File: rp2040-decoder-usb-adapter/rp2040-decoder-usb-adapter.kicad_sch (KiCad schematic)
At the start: 14 parts, among them J1 505070-2422, J2 SWD, J3 SPEAKER, J4 MISC1, J8 RAIL_PADS, P1 USB_C_Receptacle_USB2.0_16P

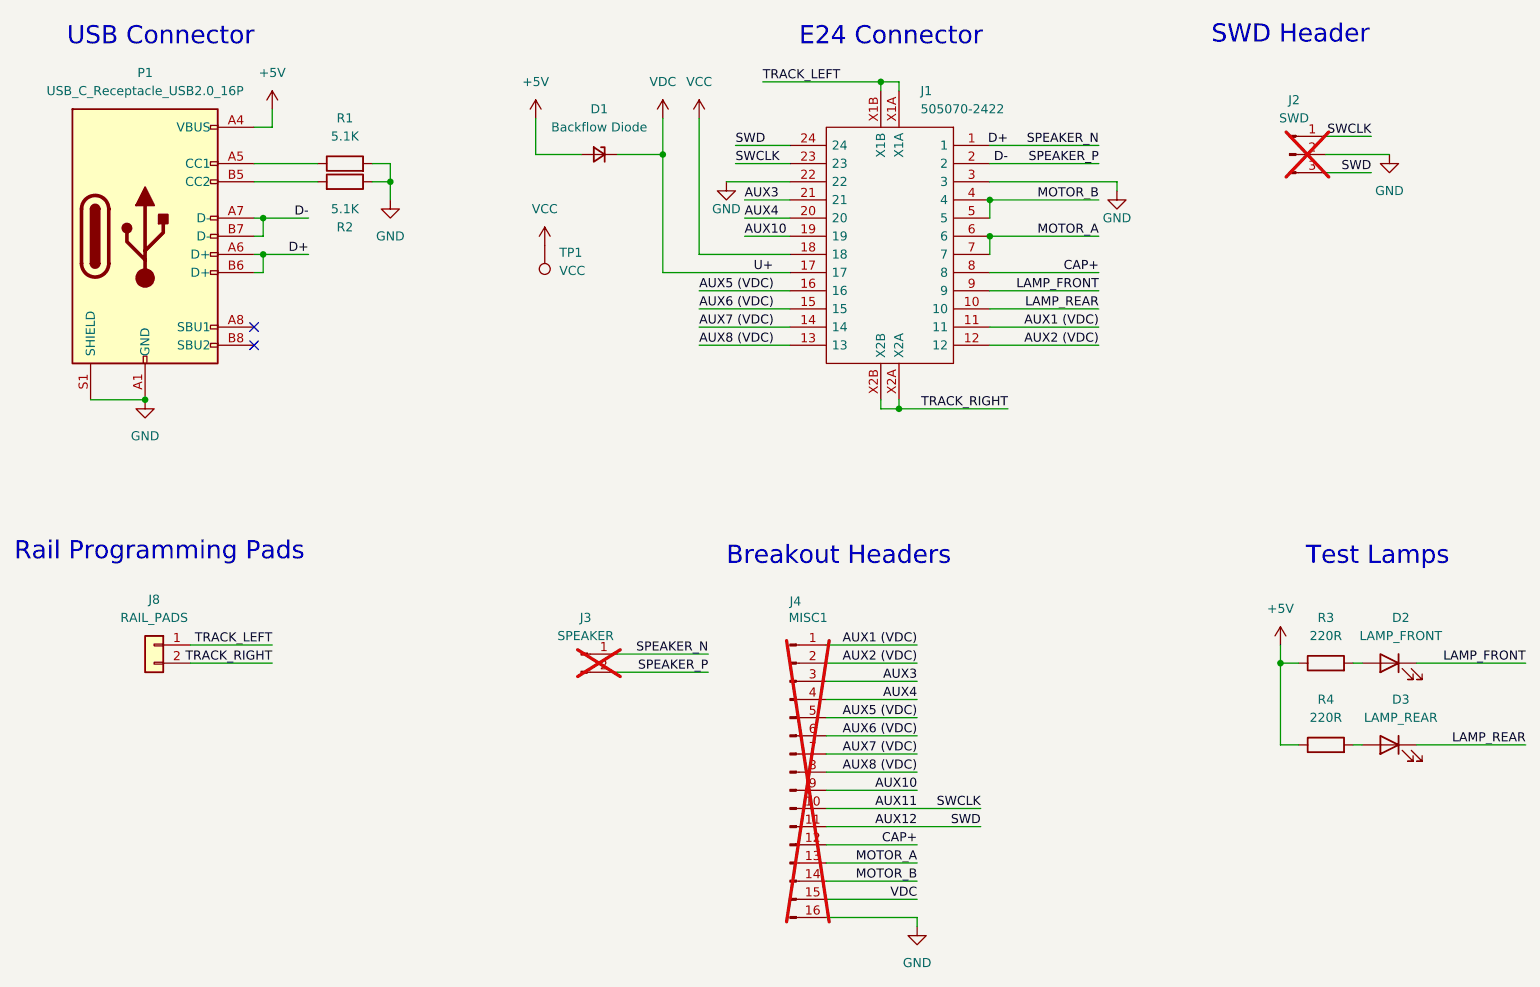
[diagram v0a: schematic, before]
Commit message: feat: move usb port to avoid shorting rails
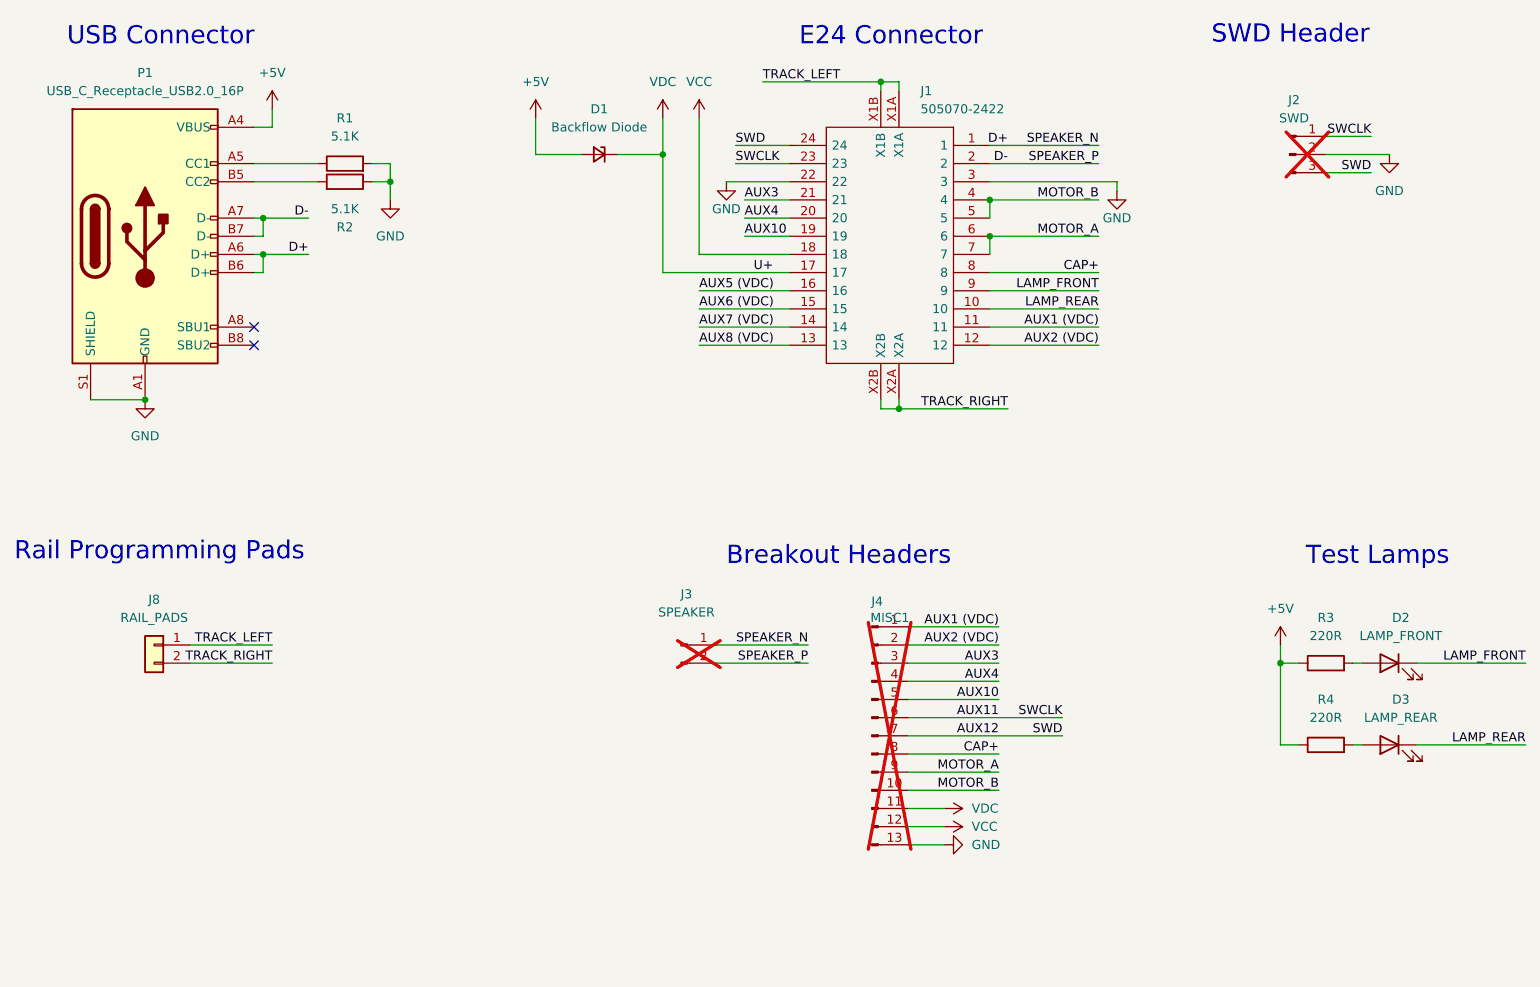
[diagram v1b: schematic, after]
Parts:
- removed TP1: VCC, TestPoint:TestPoint_Pad_3.0x3.0mm, symbol Connector:TestPoint
- J4: footprint Connector_PinHeader_2.54mm:PinHeader_1x16_P2.54mm_Vertical -> Connector_PinHeader_2.54mm:PinHeader_1x13_P2.54mm_Vertical; symbol Connector:Conn_01x16_Pin -> Connector:Conn_01x13_Pin; now in the parts list
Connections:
- net AUX10: now also J4.5 (Pin_5); no longer J4.9 (Pin_9)
- net AUX11: now also J4.6 (Pin_6); no longer J4.10 (Pin_10)
- net AUX12: now also J4.7 (Pin_7); no longer J4.11 (Pin_11)
- net AUX5 (VDC): no longer J4.5 (Pin_5)
- net AUX6 (VDC): no longer J4.6 (Pin_6)
- net AUX7 (VDC): no longer J4.7 (Pin_7)
- net AUX8 (VDC): no longer J4.8 (Pin_8)
- net CAP+: now also J4.8 (Pin_8); no longer J4.12 (Pin_12)
- net GND: now also J4.13 (Pin_13); no longer J4.16 (Pin_16)
- net MOTOR_A: now also J4.9 (Pin_9); no longer J4.13 (Pin_13)
- net MOTOR_B: now also J4.10 (Pin_10); no longer J4.14 (Pin_14)
- net VCC: now also J4.12 (Pin_12)
- net VDC: now also J4.11 (Pin_11); no longer J4.15 (Pin_15)
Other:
- moved on the sheet: J3

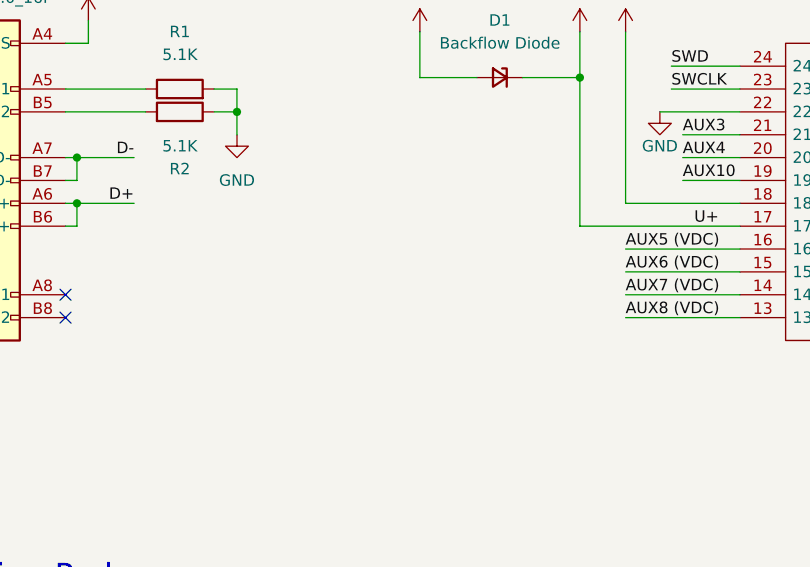
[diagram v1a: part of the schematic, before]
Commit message: feat: add external capacitor support
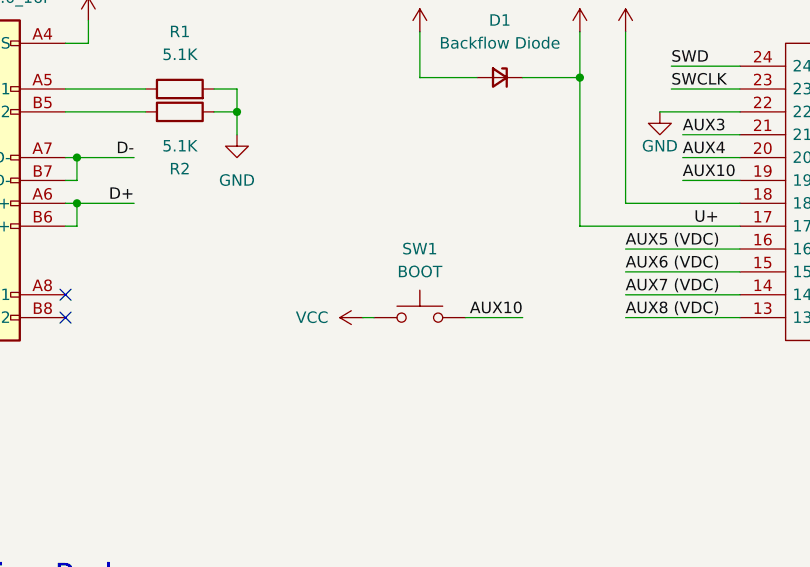
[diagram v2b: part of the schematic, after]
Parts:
- added SW1: BOOT, Local Library:Xunpu_TS-1088-AR02016, symbol Switch:SW_Push
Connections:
- net AUX10: now also SW1.2
- net VCC: now also SW1.1
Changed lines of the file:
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@@
+	(wire
+		(pts
+			(xy 106.68 83.82) (xy 107.95 83.82)
+		)
+		(stroke
+			(width 0)
+			(type default)
+		)
+	)
 	(wire
 		(pts
@@
 		(pts
 			(xy 140.97 58.42) (xy 148.59 58.42)
+		)
+		(stroke
+			(width 0)
+			(type default)
+		)
+	)
+	(wire
+		(pts
+			(xy 118.11 83.82) (xy 124.46 83.82)
 		)
 		(stroke
@@
 	(label "AUX5 (VDC)"
 		(at 135.89 76.2 0)
-		(fields_autoplaced yes)
 		(effects
 			(font
@@
 	(label "AUX10"
 		(at 142.24 68.58 0)
-		(fields_autoplaced yes)
 		(effects
 			(font
@@
 	(label "D+"
 		(at 179.07 55.88 180)
-		(fields_autoplaced yes)
 		(effects
 			(font
@@
 	(label "AUX3"
 		(at 177.8 128.27 180)
-		(fields_autoplaced yes)
 		(effects
 			(font
@@
 	(label "SWCLK"
 		(at 186.69 135.89 180)
-		(fields_autoplaced yes)
 		(effects
 			(font
@@
 	(label "AUX4"
 		(at 142.24 66.04 0)
-		(fields_autoplaced yes)
 		(effects
 			(font
@@
 	(label "MOTOR_A"
 		(at 177.8 143.51 180)
-		(fields_autoplaced yes)
 		(effects
 			(font
@@
 	(label "U+"
 		(at 143.51 73.66 0)
-		(fields_autoplaced yes)
 		(effects
 			(font
@@
 	(label "AUX7 (VDC)"
 		(at 135.89 81.28 0)
-		(fields_autoplaced yes)
 		(effects
 			(font
@@
 	(label "CAP+"
 		(at 177.8 140.97 180)
-		(fields_autoplaced yes)
 		(effects
 			(font
@@
 	(label "TRACK_LEFT"
 		(at 144.78 46.99 0)
-		(fields_autoplaced yes)
 		(effects
 			(font
@@
 	(label "AUX4"
 		(at 177.8 130.81 180)
-		(fields_autoplaced yes)
 		(effects
 			(font
@@
 	(label "TRACK_RIGHT"
 		(at 76.2 128.27 180)
-		(fields_autoplaced yes)
 		(effects
 			(font
@@
 	(label "AUX2 (VDC)"
 		(at 191.77 83.82 180)
-		(fields_autoplaced yes)
 		(effects
 			(font
@@
 	(label "SPEAKER_N"
 		(at 151.13 125.73 180)
-		(fields_autoplaced yes)
 		(effects
 			(font
@@
 	(label "D-"
 		(at 81.28 66.04 180)
-		(fields_autoplaced yes)
 		(effects
 			(font
@@
 	(label "SWCLK"
 		(at 229.87 54.61 180)
-		(fields_autoplaced yes)
 		(effects
 			(font
@@
 	(label "MOTOR_A"
 		(at 191.77 68.58 180)
-		(fields_autoplaced yes)
 		(effects
 			(font
@@
 	(label "TRACK_LEFT"
 		(at 76.2 125.73 180)
-		(fields_autoplaced yes)
 		(effects
 			(font
@@
 	(label "SPEAKER_P"
 		(at 191.77 58.42 180)
-		(fields_autoplaced yes)
 		(effects
 			(font
@@
 	(label "SWD"
 		(at 186.69 138.43 180)
-		(fields_autoplaced yes)
 		(effects
 			(font
@@
 	(label "MOTOR_B"
 		(at 191.77 63.5 180)
-		(fields_autoplaced yes)
 		(effects
 			(font
@@
 	(label "LAMP_REAR"
 		(at 251.46 139.7 180)
-		(fields_autoplaced yes)
 		(effects
 			(font
@@
 	(label "AUX1 (VDC)"
 		(at 191.77 81.28 180)
-		(fields_autoplaced yes)
 		(effects
 			(font
@@
 	(label "AUX11"
 		(at 177.8 135.89 180)
-		(fields_autoplaced yes)
 		(effects
 			(font
@@
 	(label "AUX2 (VDC)"
 		(at 177.8 125.73 180)
-		(fields_autoplaced yes)
 		(effects
 			(font
@@
 	(label "CAP+"
 		(at 191.77 73.66 180)
-		(fields_autoplaced yes)
 		(effects
 			(font
@@
 	(label "SWD"
 		(at 140.97 55.88 0)
-		(fields_autoplaced yes)
 		(effects
 			(font
@@
 	(label "SPEAKER_P"
 		(at 151.13 128.27 180)
-		(fields_autoplaced yes)
 		(effects
 			(font
@@
 	(label "AUX6 (VDC)"
 		(at 135.89 78.74 0)
-		(fields_autoplaced yes)
 		(effects
 			(font
@@
 	(label "AUX8 (VDC)"
 		(at 135.89 83.82 0)
-		(fields_autoplaced yes)
 		(effects
 			(font
@@
 	(label "LAMP_REAR"
 		(at 191.77 78.74 180)
-		(fields_autoplaced yes)
 		(effects
 			(font
@@
 	(label "SPEAKER_N"
 		(at 191.77 55.88 180)
-		(fields_autoplaced yes)
 		(effects
 			(font
@@
 	(label "LAMP_FRONT"
 		(at 251.46 128.27 180)
-		(fields_autoplaced yes)
 		(effects
 			(font
@@
 	(label "LAMP_FRONT"
 		(at 191.77 76.2 180)
-		(fields_autoplaced yes)
 		(effects
 			(font
@@
 	(label "D-"
 		(at 179.07 58.42 180)
-		(fields_autoplaced yes)
 		(effects
 			(font
@@
 	(label "AUX1 (VDC)"
 		(at 177.8 123.19 180)
-		(fields_autoplaced yes)
 		(effects
 			(font
@@
 	(label "D+"
 		(at 81.28 71.12 180)
-		(fields_autoplaced yes)
 		(effects
 			(font
@@
 	(label "SWD"
 		(at 229.87 59.69 180)
-		(fields_autoplaced yes)
 		(effects
 			(font
@@
 	(label "MOTOR_B"
 		(at 177.8 146.05 180)
-		(fields_autoplaced yes)
+		(effects
+			(font
+				(size 1.27 1.27)
+			)
+			(justify right bottom)
+		)
+	)
+	(label "AUX10"
+		(at 124.46 83.82 180)
 		(effects
 			(font
@@
 	(label "AUX10"
 		(at 177.8 133.35 180)
-		(fields_autoplaced yes)
 		(effects
 			(font
@@
 	(label "TRACK_RIGHT"
 		(at 179.07 92.71 180)
-		(fields_autoplaced yes)
 		(effects
 			(font
@@
 	(label "AUX3"
 		(at 142.24 63.5 0)
-		(fields_autoplaced yes)
 		(effects
 			(font
@@
 	(label "SWCLK"
 		(at 140.97 58.42 0)
-		(fields_autoplaced yes)
 		(effects
 			(font
@@
 	(label "AUX12"
 		(at 177.8 138.43 180)
-		(fields_autoplaced yes)
 		(effects
 			(font
@@
 	)
 	(symbol
+		(lib_id "Switch:SW_Push")
+		(at 113.03 83.82 0)
+		(unit 1)
+		(exclude_from_sim no)
+		(in_bom yes)
+		(on_board yes)
+		(dnp no)
+		(fields_autoplaced yes)
+		(property "Reference" "SW1"
+			(at 113.03 76.2 0)
+			(effects
+				(font
+					(size 1.27 1.27)
+				)
+			)
+		)
+		(property "Value" "BOOT"
+			(at 113.03 78.74 0)
+			(effects
+				(font
+					(size 1.27 1.27)
+				)
+			)
+		)
+		(property "Footprint" "Local Library:Xunpu_TS-1088-AR02016"
+			(at 113.03 78.74 0)
+			(effects
+				(font
+					(size 1.27 1.27)
+				)
+				(hide yes)
+			)
+		)
+		(property "Datasheet" "~"
+			(at 113.03 78.74 0)
+			(effects
+				(font
+					(size 1.27 1.27)
+				)
+				(hide yes)
+			)
+		)
+		(property "Description" "Push button switch, generic, two pins"
+			(at 113.03 83.82 0)
+			(effects
+				(font
+					(size 1.27 1.27)
+				)
+				(hide yes)
+			)
+		)
+		(property "LCSC" "C720477"
+			(at 113.03 83.82 0)
+			(effects
+				(font
+					(size 1.27 1.27)
+				)
+				(hide yes)
+			)
+		)
+		(pin "2"
+		)
+		(pin "1"
+		)
+		(instances
+			(project "rp2040-decoder-usb-adapter"
+				(path "/56597f90-c6fb-4200-a9c2-76774da4e426"
+					(reference "SW1")
+					(unit 1)
+				)
+			)
+		)
+	)
+	(symbol
 		(lib_name "GND_1")
 		(lib_id "power:GND")
@@
 					(unit 1)
 				)
+			)
+		)
+	)
+	(symbol
+		(lib_id "power:VCC")
+		(at 106.68 83.82 90)
+		(unit 1)
+		(exclude_from_sim no)
+		(in_bom yes)
+		(on_board yes)
+		(dnp no)
+		(fields_autoplaced yes)
+		(property "Reference" "#PWR010"
+			(at 110.49 83.82 0)
+			(effects
+				(font
+					(size 1.27 1.27)
+				)
+				(hide yes)
+			)
+		)
+		(property "Value" "VCC"
+			(at 102.87 83.8199 90)
+			(effects
+				(font
+					(size 1.27 1.27)
+				)
+				(justify left)
+			)
+		)
+		(property "Footprint" ""
+			(at 106.68 83.82 0)
+			(effects
+				(font
+					(size 1.27 1.27)
+				)
+				(hide yes)
+			)
+		)
+		(property "Datasheet" ""
+			(at 106.68 83.82 0)
+			(effects
+				(font
+					(size 1.27 1.27)
+				)
+				(hide yes)
+			)
+		)
+		(property "Description" "Power symbol creates a global label with name \"VCC\""
+			(at 106.68 83.82 0)
+			(effects
+				(font
+					(size 1.27 1.27)
+				)
+				(hide yes)
+			)
+		)
+		(pin "1"
+		)
+		(instances
+			(project "rp2040-decoder-usb-adapter"
+				(path "/56597f90-c6fb-4200-a9c2-76774da4e426"
+					(reference "#PWR010")
+					(unit 1)
+				)

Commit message: fix: make boot button easier to press
fix: dfm fixes
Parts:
- P1: JLCPCB_CORRECTION 0;-1.25;0 -> 0;-1.3;0
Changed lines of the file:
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@@
 			)
 		)
-		(property "JLCPCB_CORRECTION" "0;-1.25;0"
+		(property "JLCPCB_CORRECTION" "0;-1.3;0"
 			(at 58.42 68.58 0)
 			(effects

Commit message: fix: switch button type
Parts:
- SW1: footprint Local Library:Xunpu_TS-1088-AR02016 -> Button_Switch_SMD:SW_Push_1P1T_NO_Vertical_Wuerth_434133025816; LCSC C720477 -> C5504987
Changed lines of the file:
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@@
 			)
 		)
-		(property "Footprint" "Local Library:Xunpu_TS-1088-AR02016"
+		(property "Footprint" "Button_Switch_SMD:SW_Push_1P1T_NO_Vertical_Wuerth_434133025816"
 			(at 113.03 78.74 0)
 			(effects
@@
 			)
 		)
-		(property "LCSC" "C720477"
+		(property "LCSC" "C5504987"
 			(at 113.03 83.82 0)
 			(effects
